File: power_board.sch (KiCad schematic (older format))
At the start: 32 parts, among them CON1 MICROUSB, J1 Conn_02x03_Odd_Even, J2 Conn_01x01, J3 Conn_01x01, J4 Conn_01x01, SW1 SW_Push, U1 PCA9555PW, U2 ATMEGA328P-AU, U3 PCA9555PW, U4 FT232RL, Y1 Crystal

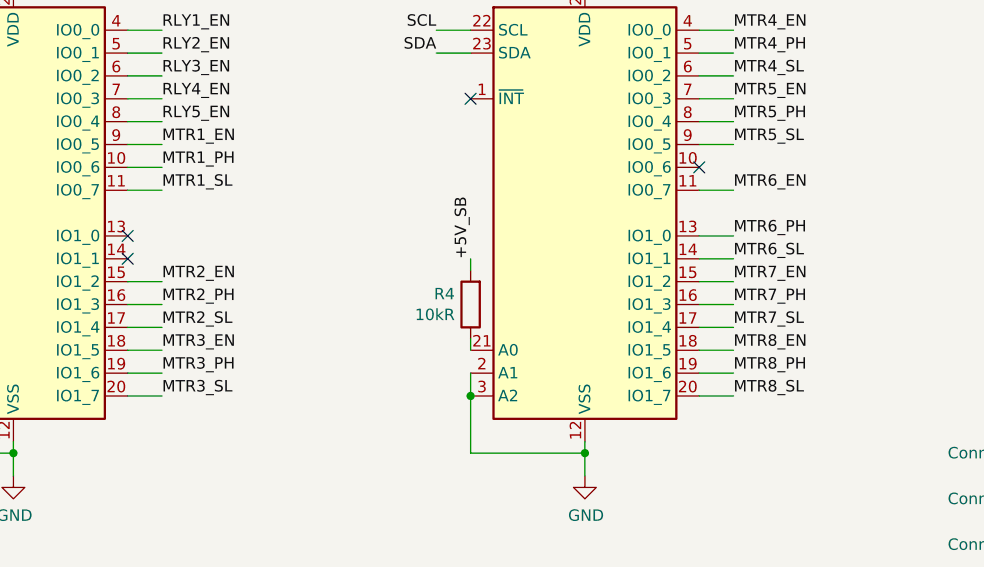
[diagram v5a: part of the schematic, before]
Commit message: Replaced FTDI placement.
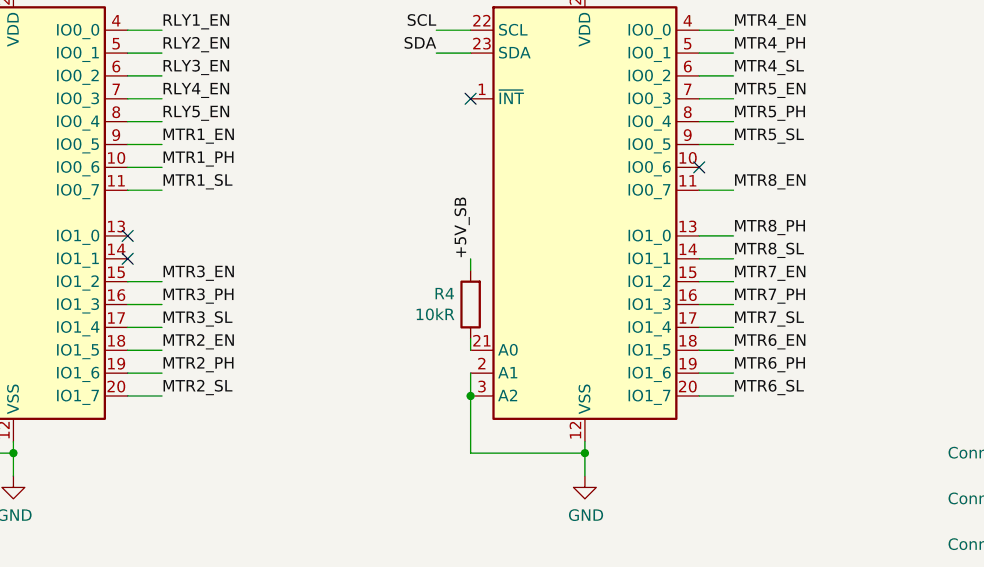
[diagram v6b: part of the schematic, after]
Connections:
- net MTR2_EN: now also U1.18 (IO1_5); no longer U1.15 (IO1_2)
- net MTR2_PH: now also U1.19 (IO1_6); no longer U1.16 (IO1_3)
- net MTR2_SL: now also U1.20 (IO1_7); no longer U1.17 (IO1_4)
- net MTR3_EN: now also U1.15 (IO1_2); no longer U1.18 (IO1_5)
- net MTR3_PH: now also U1.16 (IO1_3); no longer U1.19 (IO1_6)
- net MTR3_SL: now also U1.17 (IO1_4); no longer U1.20 (IO1_7)
- net MTR6_EN: now also U3.18 (IO1_5); no longer U3.11 (IO0_7)
- net MTR6_PH: now also U3.19 (IO1_6); no longer U3.13 (IO1_0)
- net MTR6_SL: now also U3.20 (IO1_7); no longer U3.14 (IO1_1)
- net MTR8_EN: now also U3.11 (IO0_7); no longer U3.18 (IO1_5)
- net MTR8_PH: now also U3.13 (IO1_0); no longer U3.19 (IO1_6)
- net MTR8_SL: now also U3.14 (IO1_1); no longer U3.20 (IO1_7)
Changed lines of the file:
@@
 Text Label 2400 5900 0    50   ~ 0
 MTR1_SL
+Text Label 2400 6600 0    50   ~ 0
+MTR2_EN
+Text Label 2400 6700 0    50   ~ 0
+MTR2_PH
+Text Label 2400 6800 0    50   ~ 0
+MTR2_SL
 Text Label 2400 6300 0    50   ~ 0
-MTR2_EN
-Text Label 2400 6400 0    50   ~ 0
-MTR2_PH
-Text Label 2400 6500 0    50   ~ 0
-MTR2_SL
-Text Label 2400 6600 0    50   ~ 0
 MTR3_EN
 Text Label 8750 4750 0    50   ~ 0
@@
 Text Label 8750 4550 0    50   ~ 0
 MTR5_EN
-Text Label 2400 6700 0    50   ~ 0
+Text Label 2400 6400 0    50   ~ 0
 MTR3_PH
-Text Label 2400 6800 0    50   ~ 0
+Text Label 2400 6500 0    50   ~ 0
 MTR3_SL
-Text Label 4900 5900 0    50   ~ 0
+Text Label 4900 6600 0    50   ~ 0
 MTR6_EN
-Text Label 4900 6100 0    50   ~ 0
+Text Label 4900 6700 0    50   ~ 0
 MTR6_PH
-Text Label 4900 6200 0    50   ~ 0
+Text Label 4900 6800 0    50   ~ 0
 MTR6_SL
 Text Label 4900 6300 0    50   ~ 0
@@
 Text Label 4900 6500 0    50   ~ 0
 MTR7_SL
-Text Label 4900 6600 0    50   ~ 0
+Text Label 4900 5900 0    50   ~ 0
 MTR8_EN
-Text Label 4900 6700 0    50   ~ 0
+Text Label 4900 6100 0    50   ~ 0
 MTR8_PH
-Text Label 4900 6800 0    50   ~ 0
+Text Label 4900 6200 0    50   ~ 0
 MTR8_SL
 Text Label 4900 5700 0    50   ~ 0

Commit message: Routing.
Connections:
- net MTR1_EN: now also U1.11 (IO0_7); no longer U1.9 (IO0_5)
- net MTR1_PH: now also U1.9 (IO0_5); no longer U1.10 (IO0_6)
- net MTR1_SL: now also U1.10 (IO0_6); no longer U1.11 (IO0_7)
- net MTR2_PH: now also U1.20 (IO1_7); no longer U1.19 (IO1_6)
- net MTR2_SL: now also U1.19 (IO1_6); no longer U1.20 (IO1_7)
- net MTR3_PH: now also U1.17 (IO1_4); no longer U1.16 (IO1_3)
- net MTR3_SL: now also U1.16 (IO1_3); no longer U1.17 (IO1_4)
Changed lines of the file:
@@
 Text Label 8750 5800 0    50   ~ 0
 MTR8_SL
+Text Label 2400 5900 0    50   ~ 0
+MTR1_EN
 Text Label 2400 5700 0    50   ~ 0
-MTR1_EN
+MTR1_PH
 Text Label 2400 5800 0    50   ~ 0
-MTR1_PH
-Text Label 2400 5900 0    50   ~ 0
 MTR1_SL
 Text Label 2400 6600 0    50   ~ 0
 MTR2_EN
+Text Label 2400 6800 0    50   ~ 0
+MTR2_PH
 Text Label 2400 6700 0    50   ~ 0
-MTR2_PH
-Text Label 2400 6800 0    50   ~ 0
 MTR2_SL
 Text Label 2400 6300 0    50   ~ 0
@@
 Text Label 8750 4550 0    50   ~ 0
 MTR5_EN
+Text Label 2400 6500 0    50   ~ 0
+MTR3_PH
 Text Label 2400 6400 0    50   ~ 0
-MTR3_PH
-Text Label 2400 6500 0    50   ~ 0
 MTR3_SL
 Text Label 4900 6600 0    50   ~ 0

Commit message: New driver arrangement
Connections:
- net MTR4_EN: now also U3.6 (IO0_2); no longer U3.4 (IO0_0)
- net MTR4_PH: now also U3.4 (IO0_0); no longer U3.5 (IO0_1)
- net MTR4_SL: now also U3.5 (IO0_1); no longer U3.6 (IO0_2)
- net MTR5_EN: now also U3.9 (IO0_5); no longer U3.7 (IO0_3)
- net MTR5_PH: now also U3.7 (IO0_3); no longer U3.8 (IO0_4)
- net MTR5_SL: now also U3.8 (IO0_4); no longer U3.9 (IO0_5)
- net MTR6_PH: now also U3.20 (IO1_7); no longer U3.19 (IO1_6)
- net MTR6_SL: now also U3.19 (IO1_6); no longer U3.20 (IO1_7)
- net MTR7_PH: now also U3.17 (IO1_4); no longer U3.16 (IO1_3)
- net MTR7_SL: now also U3.16 (IO1_3); no longer U3.17 (IO1_4)
- net MTR8_PH: now also U3.14 (IO1_1); no longer U3.13 (IO1_0)
- net MTR8_SL: now also U3.13 (IO1_0); no longer U3.14 (IO1_1)
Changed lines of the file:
@@
 Text Label 4900 6600 0    50   ~ 0
 MTR6_EN
+Text Label 4900 6800 0    50   ~ 0
+MTR6_PH
 Text Label 4900 6700 0    50   ~ 0
-MTR6_PH
-Text Label 4900 6800 0    50   ~ 0
 MTR6_SL
 Text Label 4900 6300 0    50   ~ 0
 MTR7_EN
+Text Label 4900 6500 0    50   ~ 0
+MTR7_PH
 Text Label 4900 6400 0    50   ~ 0
-MTR7_PH
-Text Label 4900 6500 0    50   ~ 0
 MTR7_SL
 Text Label 4900 5900 0    50   ~ 0
 MTR8_EN
+Text Label 4900 6200 0    50   ~ 0
+MTR8_PH
 Text Label 4900 6100 0    50   ~ 0
-MTR8_PH
-Text Label 4900 6200 0    50   ~ 0
 MTR8_SL
+Text Label 4900 5600 0    50   ~ 0
+MTR5_SL
+Text Label 4900 5500 0    50   ~ 0
+MTR5_PH
 Text Label 4900 5700 0    50   ~ 0
-MTR5_SL
-Text Label 4900 5600 0    50   ~ 0
-MTR5_PH
-Text Label 4900 5500 0    50   ~ 0
 MTR5_EN
+Text Label 4900 5400 0    50   ~ 0
+MTR4_EN
 Text Label 4900 5200 0    50   ~ 0
-MTR4_EN
+MTR4_PH
 Text Label 4900 5300 0    50   ~ 0
-MTR4_PH
-Text Label 4900 5400 0    50   ~ 0
 MTR4_SL
 $EndSCHEMATC
